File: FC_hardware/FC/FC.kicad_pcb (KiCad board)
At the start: 4 copper layers, 34 x 34 mm, 82 parts, among them J1 Pin_01x04, J10 GND, J11 GND, J12 GND, J13 Pin_02x03, J14 Pin_01x03, J15 Pin_01x03, J16 PB2, J17 PC9, J18 PC8, J19 PB7, J2 USB4105GFA120, J20 PB6, J21 PA8, J22 PC11, J23 PC10, J24 PC12, J25 PB10, J26 PC7, J27 PC6, J3 530480810, J4 BAT, J5 5V, J6 5V, J7 3V3, J8 3V3, J9 GND, Q1 BC807W, U1 MP2348, U2 AMS1117-3.3, U3 STM32F446RETx, U4 MPU-9250, U5 DPS368XTSA1, U6 Ai-Thinker-Ra-02, Y1 ABM8G-25MHZ

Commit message: Layout pcb
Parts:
- added C19: 0.1uF, Capacitor_SMD:C_0603_1608Metric, B.Cu at (106.3, 117.8)
- added C20: 0.1uF, Capacitor_SMD:C_0603_1608Metric, B.Cu at (120.6, 126.2)
- added C21: 0.1uF, Capacitor_SMD:C_0603_1608Metric, B.Cu at (108.8, 128.2)
- added C22: 0.1uF, Capacitor_SMD:C_0603_1608Metric, B.Cu at (121.5, 118.3)
- C10, C11, C15, C17, C5, C7, C8, C9, D2, D3, J2, JP1, JP2, R12, R13, R14, R6, R7, R8, R9, S1, U2, U3, U5, Y1: moved to B.Cu
- moved U3 85.7 mm to (113.8, 121.3), turned to -90 degrees
- moved R7 83.3 mm to (103.5, 119.8), turned to 180 degrees
- moved C13 81.3 mm to (100.8, 124.0), turned to -90 degrees
- moved C12 80.3 mm to (103.8, 126.3)
- moved U5 77.5 mm to (116.8, 130.2)
- moved R17 77.0 mm to (109.1, 112.2), turned to 180 degrees
- moved L1 76.3 mm to (120.8, 108.8), turned to -90 degrees
- moved Q1 75.7 mm to (110.6, 109.9), turned to 90 degrees
- moved R18 75.1 mm to (110.2, 107.6)
- moved U4 74.6 mm to (103.8, 123.3), turned to -90 degrees
- moved R15 74.1 mm to (112.5, 110.7), turned to -90 degrees
- moved C9 73.5 mm to (109.7, 112.9), turned to 90 degrees
- moved C14 73.5 mm to (107.0, 120.8), turned to 90 degrees
- moved R16 73.4 mm to (112.5, 108.9), turned to 90 degrees
- moved R14 73.3 mm to (120.7, 128.8), turned to -90 degrees
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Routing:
- net GND: track 0.00 -> 79.0 mm, vias 0 -> 36
- net 3V3: track 0.00 -> 50.4 mm, vias 0 -> 22
- net /USB_DM: track 0.00 -> 45.0 mm, vias 0 -> 4
- net 5V: track 0.00 -> 44.9 mm, vias 0 -> 2
- net /USB_DP: track 0.00 -> 42.5 mm, vias 0 -> 4
- net Net-(U3-NRST): track 0.00 -> 25.2 mm, vias 0 -> 2
- net BAT: track 0.00 -> 24.5 mm, vias 0 -> 1
- net /GEN_SCL: track 0.00 -> 22.8 mm, vias 0 -> 2
- net /SWDIO: track 0.00 -> 21.0 mm, vias 0 -> 1
- net /GEN_MOSI: track 0.00 -> 20.4 mm, vias 0 -> 2
- net /BAR_CSB: track 0.00 -> 19.1 mm, vias 0 -> 2
- net /LORA_BAR_MOSI: track 0.00 -> 17.6 mm, vias 0 -> 3
- net /SBUS_RX: track 0.00 -> 17.6 mm, vias 0 -> 3
- net /GEN_RX: track 0.00 -> 17.0 mm, vias 0 -> 2
- net /GEN_TX: track 0.00 -> 16.8 mm, vias 0 -> 2
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- added copper zone on In1.Cu, net 3V3
- added copper zone on In2.Cu, net GND

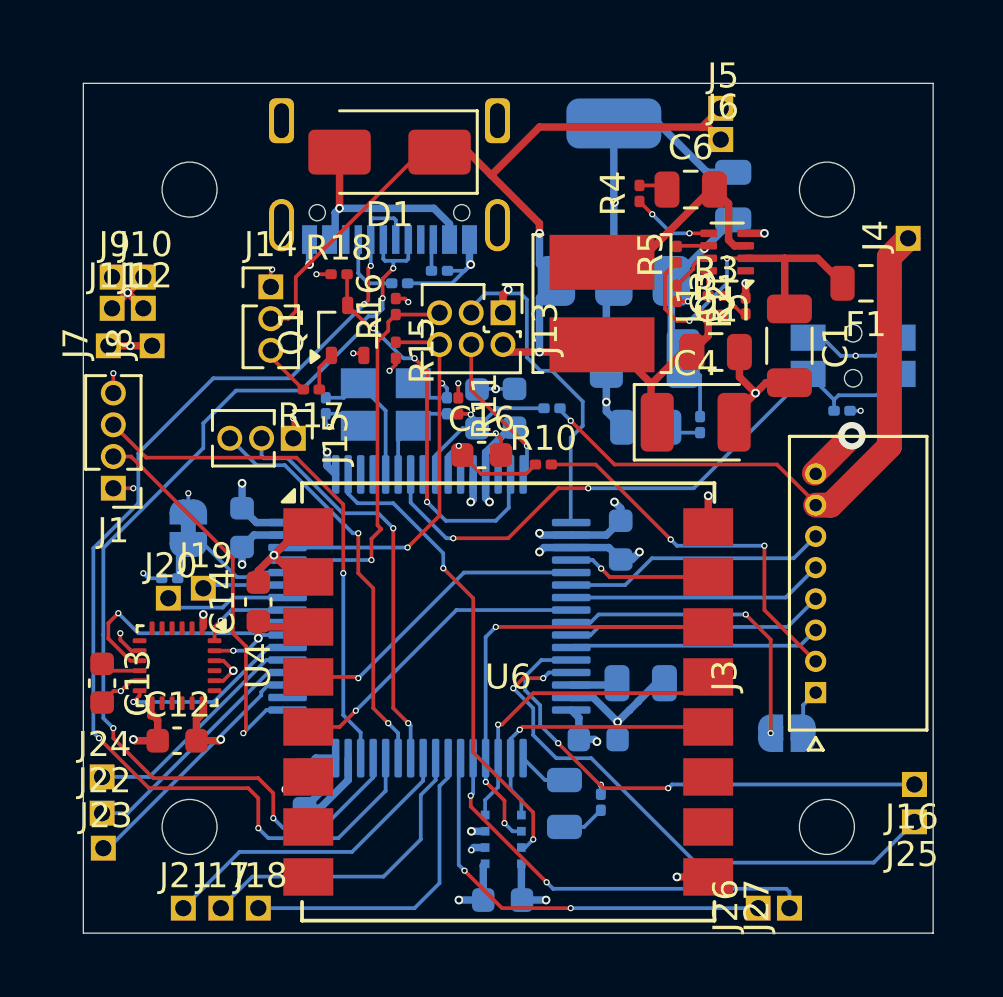
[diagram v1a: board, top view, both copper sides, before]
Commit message: Round corners, fix some DRC violations
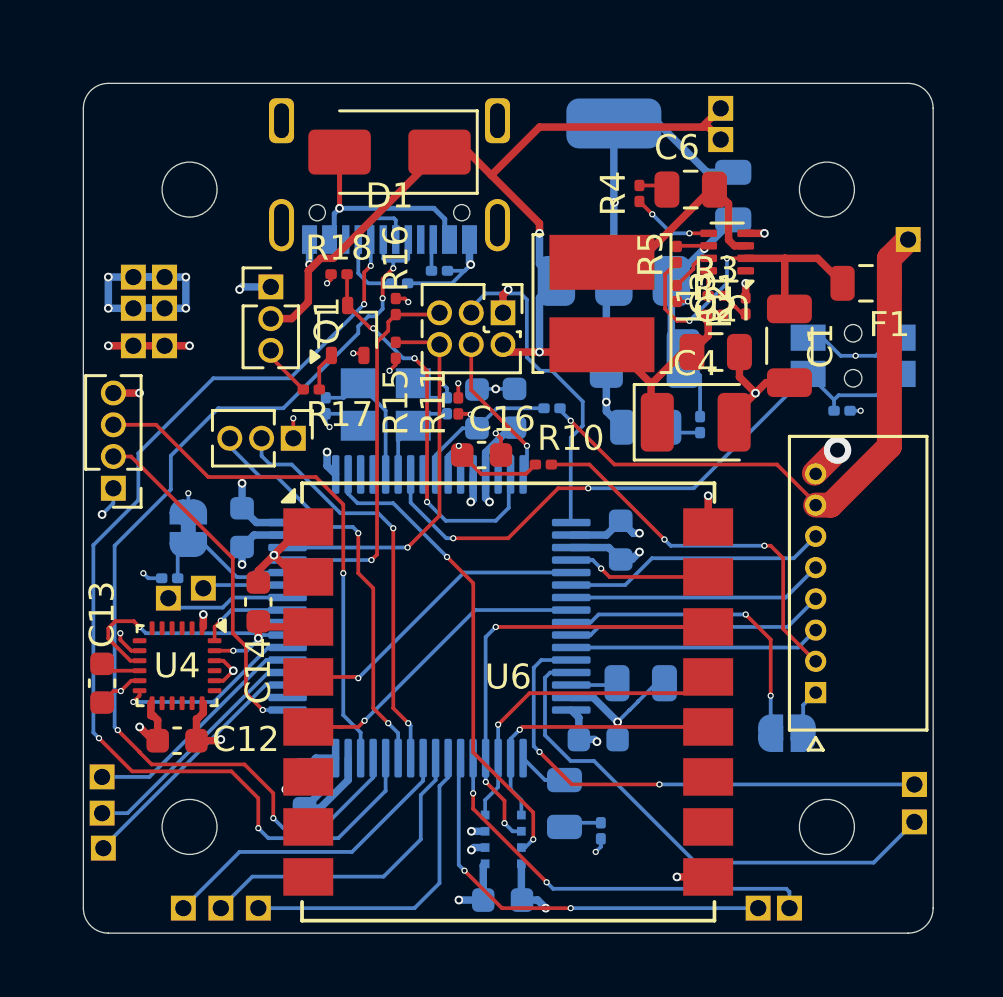
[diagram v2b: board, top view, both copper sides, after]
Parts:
- moved R14 1.14 mm to (120.7, 129.9), turned to 90 degrees
- moved J7 1.00 mm to (102.0, 110.5)
- moved J10 0.85 mm to (103.2, 107.8)
- moved J11 0.85 mm to (102.0, 109.0)
- moved J12 0.85 mm to (103.2, 109.0)
- moved J9 0.85 mm to (102.0, 107.8)
- moved J8 0.50 mm to (103.2, 110.5)
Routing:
- net GND: track 79.0 -> 85.6 mm, vias 36 -> 38
- net /SWCLK: track 15.9 -> 14.0 mm
- net /GEN_SCL: track 22.8 -> 21.0 mm, vias 2 -> 0
- net /USB_DP: track 42.5 -> 41.8 mm
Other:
- outline, holes or cut-outs redrawn

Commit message: Fix some via and silkscreen issues
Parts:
- JP1, R7: moved to F.Cu
- moved J19 2.72 mm to (102.2, 119.2)
- moved J20 1.15 mm to (102.2, 120.5)
- moved R7 1.06 mm to (103.9, 120.8)
- moved JP1 0.90 mm to (104.5, 118.7)
- moved R12 0.34 mm to (118.8, 113.3), turned to 90 degrees
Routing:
- net /TIM4_2: track 3.42 -> 6.26 mm
- net 3V3: track 50.8 -> 49.3 mm, vias 22 -> 23
- net GND: track 85.6 -> 84.3 mm
- net /TIM4_1: track 5.09 -> 5.95 mm
- net /USB_DP: track 41.8 -> 41.0 mm
- net /USB_DM: track 45.0 -> 44.3 mm
- net Net-(JP1-B): track 6.11 -> 5.49 mm, vias 0 -> 1
- net /SWCLK: track 14.0 -> 14.6 mm
